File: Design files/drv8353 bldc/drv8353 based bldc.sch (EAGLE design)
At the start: 123 parts, among them IC1 DRV8353RSRGZT, J3 2X6 FEMALE, J4 B06B-HCMKK

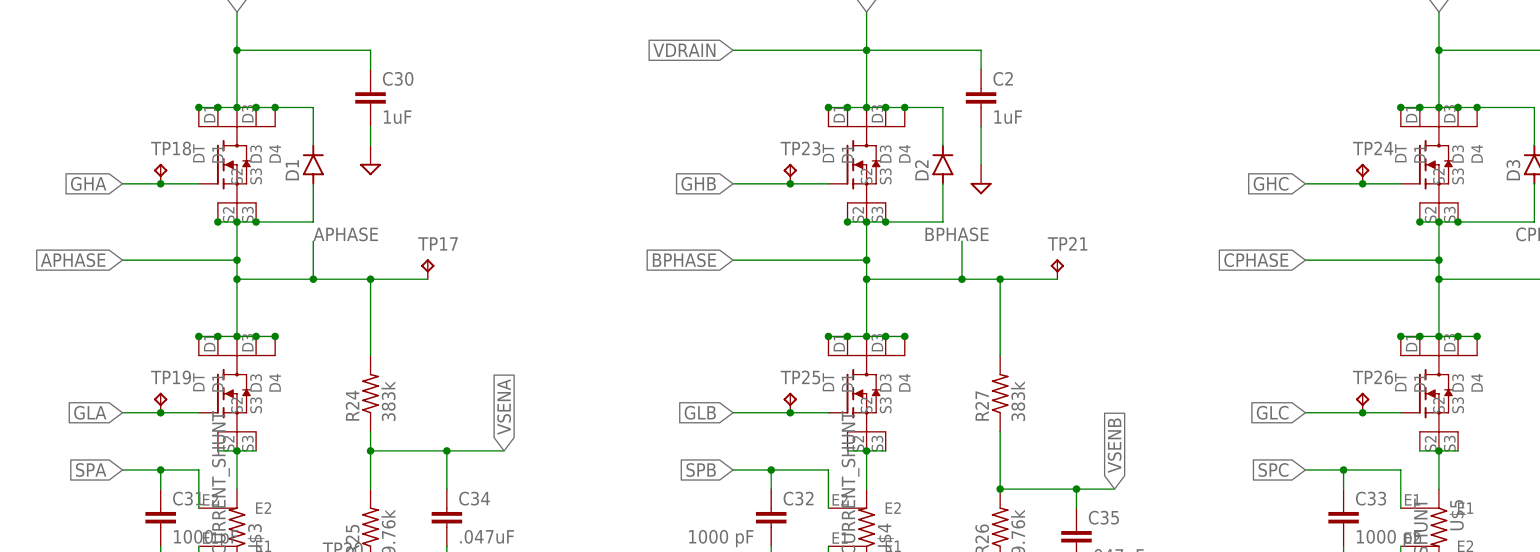
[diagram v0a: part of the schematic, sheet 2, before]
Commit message: placed most test points
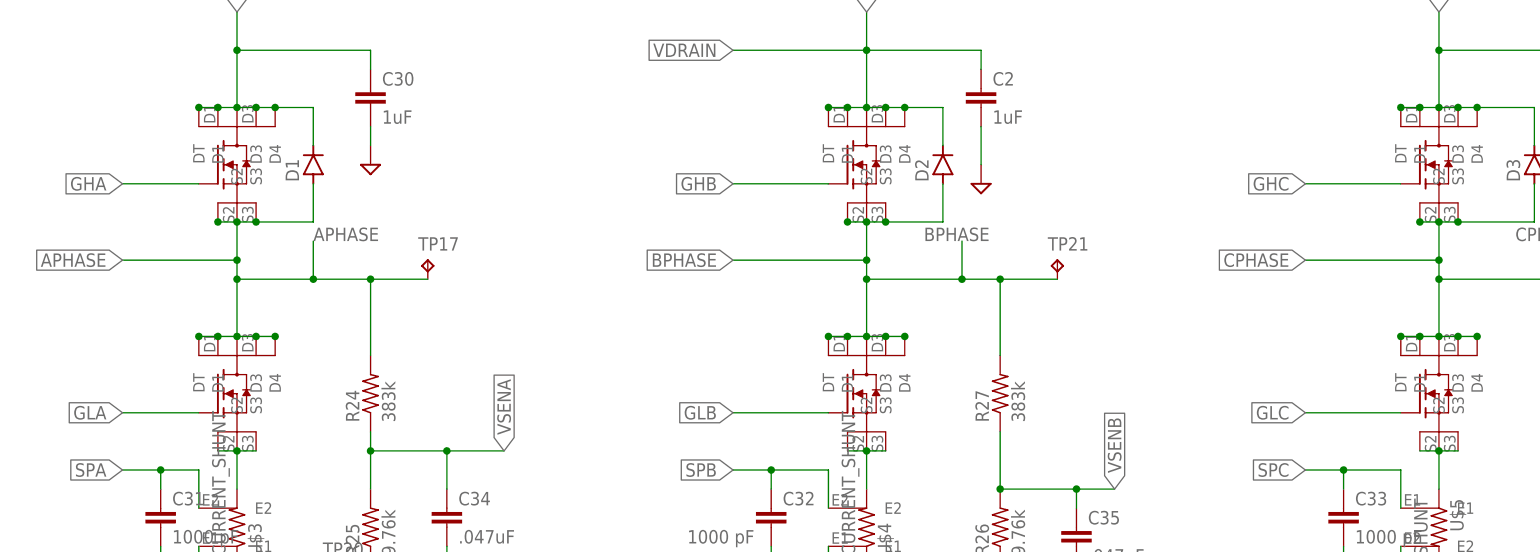
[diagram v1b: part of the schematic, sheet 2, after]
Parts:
- removed TP19, TP23, TP24, TP25, TP26: TPB1,27, testpad:TPB1,27
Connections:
- net GHA: no longer TP18.TP
- net GHB: no longer TP23.TP
- net GHC: no longer TP24.TP
- net GLA: no longer TP19.TP
- net GLB: no longer TP25.TP
- net GLC: no longer TP26.TP
- net SOA: now also TP18.TP
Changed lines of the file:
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@@
 <part name="U$24" library="REV BLDC" deviceset="NVMTS1D2N08H" device=""/>
 <part name="TP17" library="testpad" library_urn="urn:adsk.eagle:library:385" deviceset="TP" device="B1,27" package3d_urn="urn:adsk.eagle:package:27944/2"/>
-<part name="TP18" library="testpad" library_urn="urn:adsk.eagle:library:385" deviceset="TP" device="B1,27" package3d_urn="urn:adsk.eagle:package:27944/2"/>
-<part name="TP19" library="testpad" library_urn="urn:adsk.eagle:library:385" deviceset="TP" device="B1,27" package3d_urn="urn:adsk.eagle:package:27944/2"/>
 <part name="C30" library="rcl" library_urn="urn:adsk.eagle:library:334" deviceset="C-EU" device="C1206" package3d_urn="urn:adsk.eagle:package:23618/2" value="1uF"/>
 <part name="C31" library="rcl" library_urn="urn:adsk.eagle:library:334" deviceset="C-EU" device="C0603K" package3d_urn="urn:adsk.eagle:package:23680/2" value="1000 pF"/>
@@
 <part name="R29" library="rcl" library_urn="urn:adsk.eagle:library:334" deviceset="R-US_" device="R0603" package3d_urn="urn:adsk.eagle:package:23555/3" value="9.76k"/>
 <part name="C36" library="rcl" library_urn="urn:adsk.eagle:library:334" deviceset="C-EU" device="C0603K" package3d_urn="urn:adsk.eagle:package:23680/2" value=".047uF"/>
-<part name="TP23" library="testpad" library_urn="urn:adsk.eagle:library:385" deviceset="TP" device="B1,27" package3d_urn="urn:adsk.eagle:package:27944/2"/>
-<part name="TP24" library="testpad" library_urn="urn:adsk.eagle:library:385" deviceset="TP" device="B1,27" package3d_urn="urn:adsk.eagle:package:27944/2"/>
-<part name="TP25" library="testpad" library_urn="urn:adsk.eagle:library:385" deviceset="TP" device="B1,27" package3d_urn="urn:adsk.eagle:package:27944/2"/>
-<part name="TP26" library="testpad" library_urn="urn:adsk.eagle:library:385" deviceset="TP" device="B1,27" package3d_urn="urn:adsk.eagle:package:27944/2"/>
 <part name="TP27" library="testpad" library_urn="urn:adsk.eagle:library:385" deviceset="TP" device="B1,27" package3d_urn="urn:adsk.eagle:package:27944/2"/>
 <part name="TP28" library="testpad" library_urn="urn:adsk.eagle:library:385" deviceset="TP" device="B1,27" package3d_urn="urn:adsk.eagle:package:27944/2"/>
@@
 <part name="C3" library="rcl" library_urn="urn:adsk.eagle:library:334" deviceset="C-EU" device="C1206" package3d_urn="urn:adsk.eagle:package:23618/2" value="1uF"/>
 <part name="TP40" library="testpad" library_urn="urn:adsk.eagle:library:385" deviceset="TP" device="B1,27" package3d_urn="urn:adsk.eagle:package:27944/2"/>
+<part name="TP18" library="testpad" library_urn="urn:adsk.eagle:library:385" deviceset="TP" device="B1,27" package3d_urn="urn:adsk.eagle:package:27944/2"/>
 </parts>
 <sheets>
@@
 <attribute name="TP_SIGNAL_NAME" x="-67.31" y="-82.55" size="1.778" layer="97"/>
 </instance>
+<instance part="TP18" gate="G$1" x="48.26" y="-71.12" smashed="yes" rot="R180">
+<attribute name="NAME" x="49.53" y="-72.39" size="1.778" layer="95" rot="R180"/>
+<attribute name="TP_SIGNAL_NAME" x="46.99" y="-69.85" size="1.778" layer="97" rot="R180"/>
+</instance>
 </instances>
 <busses>
@@
 <wire x1="43.18" y1="-68.58" x2="48.26" y2="-68.58" width="0.1524" layer="91"/>
 <label x="48.26" y="-68.58" size="1.778" layer="95"/>
+<pinref part="TP18" gate="G$1" pin="TP"/>
 </segment>
 </net>
@@
 <attribute name="TP_SIGNAL_NAME" x="-29.21" y="46.99" size="1.778" layer="97"/>
 </instance>
-<instance part="TP18" gate="G$1" x="-66.04" y="60.96" smashed="yes">
-<attribute name="NAME" x="-67.31" y="62.23" size="1.778" layer="95"/>
-<attribute name="TP_SIGNAL_NAME" x="-64.77" y="59.69" size="1.778" layer="97"/>
-</instance>
-<instance part="TP19" gate="G$1" x="-66.04" y="30.48" smashed="yes">
-<attribute name="NAME" x="-67.31" y="31.75" size="1.778" layer="95"/>
-<attribute name="TP_SIGNAL_NAME" x="-64.77" y="29.21" size="1.778" layer="97"/>
-</instance>
 <instance part="C30" gate="G$1" x="-38.1" y="71.12" smashed="yes">
 <attribute name="NAME" x="-36.576" y="71.501" size="1.778" layer="95"/>
@@
 <attribute name="NAME" x="141.224" y="15.621" size="1.778" layer="95"/>
 <attribute name="VALUE" x="141.224" y="10.541" size="1.778" layer="96"/>
-</instance>
-<instance part="TP23" gate="G$1" x="17.78" y="60.96" smashed="yes">
-<attribute name="NAME" x="16.51" y="62.23" size="1.778" layer="95"/>
-<attribute name="TP_SIGNAL_NAME" x="19.05" y="59.69" size="1.778" layer="97"/>
-</instance>
-<instance part="TP24" gate="G$1" x="93.98" y="60.96" smashed="yes">
-<attribute name="NAME" x="92.71" y="62.23" size="1.778" layer="95"/>
-<attribute name="TP_SIGNAL_NAME" x="95.25" y="59.69" size="1.778" layer="97"/>
-</instance>
-<instance part="TP25" gate="G$1" x="17.78" y="30.48" smashed="yes">
-<attribute name="NAME" x="16.51" y="31.75" size="1.778" layer="95"/>
-<attribute name="TP_SIGNAL_NAME" x="19.05" y="29.21" size="1.778" layer="97"/>
-</instance>
-<instance part="TP26" gate="G$1" x="93.98" y="30.48" smashed="yes">
-<attribute name="NAME" x="92.71" y="31.75" size="1.778" layer="95"/>
-<attribute name="TP_SIGNAL_NAME" x="95.25" y="29.21" size="1.778" layer="97"/>
 </instance>
 <instance part="TP27" gate="G$1" x="40.64" y="7.62" smashed="yes">
@@
 <segment>
 <pinref part="U$14" gate="G$1" pin="G"/>
-<wire x1="-60.96" y1="58.42" x2="-66.04" y2="58.42" width="0.1524" layer="91"/>
-<pinref part="TP18" gate="G$1" pin="TP"/>
-<wire x1="-66.04" y1="58.42" x2="-71.12" y2="58.42" width="0.1524" layer="91"/>
-<junction x="-66.04" y="58.42"/>
+<wire x1="-60.96" y1="58.42" x2="-71.12" y2="58.42" width="0.1524" layer="91"/>
 <label x="-71.12" y="58.42" size="1.778" layer="95" rot="R180" xref="yes"/>
 </segment>
@@
 <segment>
 <pinref part="U$20" gate="G$1" pin="G"/>
-<wire x1="-60.96" y1="27.94" x2="-66.04" y2="27.94" width="0.1524" layer="91"/>
-<pinref part="TP19" gate="G$1" pin="TP"/>
-<wire x1="-66.04" y1="27.94" x2="-71.12" y2="27.94" width="0.1524" layer="91"/>
-<junction x="-66.04" y="27.94"/>
+<wire x1="-60.96" y1="27.94" x2="-71.12" y2="27.94" width="0.1524" layer="91"/>
 <label x="-71.12" y="27.94" size="1.778" layer="95" rot="R180" xref="yes"/>
 </segment>
@@
 <segment>
 <pinref part="U$22" gate="G$1" pin="G"/>
-<wire x1="22.86" y1="58.42" x2="17.78" y2="58.42" width="0.1524" layer="91"/>
-<pinref part="TP23" gate="G$1" pin="TP"/>
-<wire x1="17.78" y1="58.42" x2="10.16" y2="58.42" width="0.1524" layer="91"/>
-<junction x="17.78" y="58.42"/>
+<wire x1="22.86" y1="58.42" x2="10.16" y2="58.42" width="0.1524" layer="91"/>
 <label x="10.16" y="58.42" size="1.778" layer="95" rot="R180" xref="yes"/>
 </segment>
@@
 <segment>
 <pinref part="U$21" gate="G$1" pin="G"/>
-<wire x1="22.86" y1="27.94" x2="17.78" y2="27.94" width="0.1524" layer="91"/>
-<pinref part="TP25" gate="G$1" pin="TP"/>
-<wire x1="17.78" y1="27.94" x2="10.16" y2="27.94" width="0.1524" layer="91"/>
-<junction x="17.78" y="27.94"/>
+<wire x1="22.86" y1="27.94" x2="10.16" y2="27.94" width="0.1524" layer="91"/>
 <label x="10.16" y="27.94" size="1.778" layer="95" rot="R180" xref="yes"/>
 </segment>
@@
 <segment>
 <pinref part="U$24" gate="G$1" pin="G"/>
-<wire x1="99.06" y1="27.94" x2="93.98" y2="27.94" width="0.1524" layer="91"/>
-<pinref part="TP26" gate="G$1" pin="TP"/>
-<wire x1="93.98" y1="27.94" x2="86.36" y2="27.94" width="0.1524" layer="91"/>
-<junction x="93.98" y="27.94"/>
+<wire x1="99.06" y1="27.94" x2="86.36" y2="27.94" width="0.1524" layer="91"/>
 <label x="86.36" y="27.94" size="1.778" layer="95" rot="R180" xref="yes"/>
 </segment>
@@
 <segment>
 <pinref part="U$23" gate="G$1" pin="G"/>
-<wire x1="99.06" y1="58.42" x2="93.98" y2="58.42" width="0.1524" layer="91"/>
-<pinref part="TP24" gate="G$1" pin="TP"/>
-<wire x1="93.98" y1="58.42" x2="86.36" y2="58.42" width="0.1524" layer="91"/>
-<junction x="93.98" y="58.42"/>
+<wire x1="99.06" y1="58.42" x2="86.36" y2="58.42" width="0.1524" layer="91"/>
 <label x="86.36" y="58.42" size="1.778" layer="95" rot="R180" xref="yes"/>
 </segment>

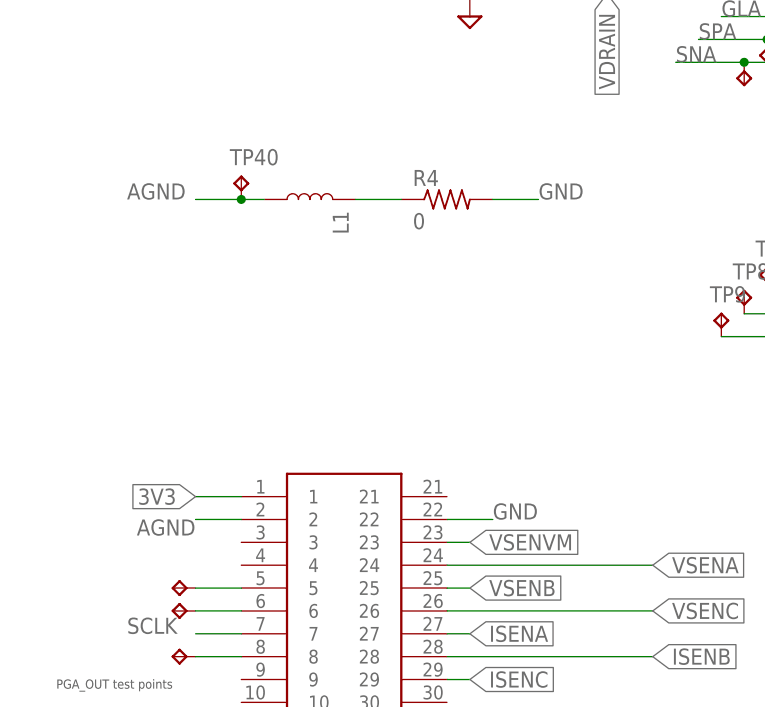
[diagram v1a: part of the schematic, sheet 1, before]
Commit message: fixes: c31-33 closer to fets, spacing of ABCPhases, layout of drv internal buck regulator
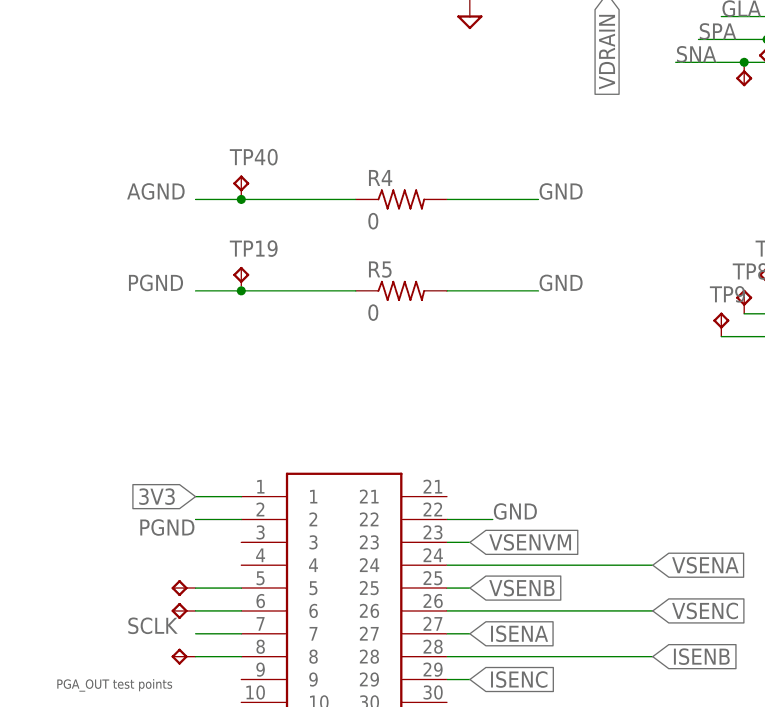
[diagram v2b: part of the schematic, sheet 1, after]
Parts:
- removed L1: 33nH/±5%/500mA, SparkFun-Coils:INDUCTOR-0603-33NH
- added R5: 0, resistor:R-US_R0603
- added TP19: TPB1,27, testpad:TPB1,27
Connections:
- removed net N$21: L1.2, R4.1
- new net PGND: R5.1, TP19.TP, U$2.2
- net AGND: now also R4.1; no longer L1.1, U$2.2
- net GND: now also R5.2
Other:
- moved on the sheet: R4
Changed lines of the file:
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@@
 <?xml version="1.0" encoding="utf-8"?>
 <!DOCTYPE eagle SYSTEM "eagle.dtd">
-<eagle version="9.5.0">
+<eagle version="9.5.1">
 <drawing>
 <settings>
@@
 <part name="SUPPLY11" library="supply2" library_urn="urn:adsk.eagle:library:372" deviceset="GND" device=""/>
 <part name="R3" library="resistor" library_urn="urn:adsk.eagle:library:348" deviceset="R-US_" device="R0603" package3d_urn="urn:adsk.eagle:package:26057/1" value="5K"/>
-<part name="L1" library="SparkFun-Coils" library_urn="urn:adsk.eagle:library:512" deviceset="INDUCTOR" device="-0603-33NH" package3d_urn="urn:adsk.eagle:package:37574/1" value="33nH/±5%/500mA"/>
 <part name="R4" library="resistor" library_urn="urn:adsk.eagle:library:348" deviceset="R-US_" device="R0603" package3d_urn="urn:adsk.eagle:package:26057/1" value="0"/>
 <part name="U$3" library="REV BLDC" deviceset="CURRENT_SHUNT" device=""/>
@@
 <part name="TP40" library="testpad" library_urn="urn:adsk.eagle:library:385" deviceset="TP" device="B1,27" package3d_urn="urn:adsk.eagle:package:27944/2"/>
 <part name="TP18" library="testpad" library_urn="urn:adsk.eagle:library:385" deviceset="TP" device="B1,27" package3d_urn="urn:adsk.eagle:package:27944/2"/>
+<part name="R5" library="resistor" library_urn="urn:adsk.eagle:library:348" deviceset="R-US_" device="R0603" package3d_urn="urn:adsk.eagle:package:26057/1" value="0"/>
+<part name="TP19" library="testpad" library_urn="urn:adsk.eagle:library:385" deviceset="TP" device="B1,27" package3d_urn="urn:adsk.eagle:package:27944/2"/>
 </parts>
 <sheets>
@@
 <attribute name="VALUE" x="92.71" y="-127.762" size="1.778" layer="96"/>
 </instance>
-<instance part="L1" gate="G$1" x="-60.96" y="-83.82" smashed="yes" rot="R90">
-<attribute name="NAME" x="-58.42" y="-85.09" size="1.778" layer="95" rot="R270"/>
-</instance>
-<instance part="R4" gate="G$1" x="-45.72" y="-83.82" smashed="yes">
-<attribute name="NAME" x="-49.53" y="-82.3214" size="1.778" layer="95"/>
-<attribute name="VALUE" x="-49.53" y="-87.122" size="1.778" layer="96"/>
+<instance part="R4" gate="G$1" x="-50.8" y="-83.82" smashed="yes">
+<attribute name="NAME" x="-54.61" y="-82.3214" size="1.778" layer="95"/>
+<attribute name="VALUE" x="-54.61" y="-87.122" size="1.778" layer="96"/>
 </instance>
 <instance part="TP40" gate="G$1" x="-68.58" y="-81.28" smashed="yes">
@@
 <attribute name="NAME" x="49.53" y="-72.39" size="1.778" layer="95" rot="R180"/>
 <attribute name="TP_SIGNAL_NAME" x="46.99" y="-69.85" size="1.778" layer="97" rot="R180"/>
+</instance>
+<instance part="R5" gate="G$1" x="-50.8" y="-93.98" smashed="yes">
+<attribute name="NAME" x="-54.61" y="-92.4814" size="1.778" layer="95"/>
+<attribute name="VALUE" x="-54.61" y="-97.282" size="1.778" layer="96"/>
+</instance>
+<instance part="TP19" gate="G$1" x="-68.58" y="-91.44" smashed="yes">
+<attribute name="NAME" x="-69.85" y="-90.17" size="1.778" layer="95"/>
+<attribute name="TP_SIGNAL_NAME" x="-67.31" y="-92.71" size="1.778" layer="97"/>
 </instance>
 </instances>
@@
 <segment>
 <pinref part="R4" gate="G$1" pin="2"/>
-<wire x1="-40.64" y1="-83.82" x2="-35.56" y2="-83.82" width="0.1524" layer="91"/>
+<wire x1="-45.72" y1="-83.82" x2="-35.56" y2="-83.82" width="0.1524" layer="91"/>
 <label x="-35.56" y="-83.82" size="1.778" layer="95"/>
 </segment>
@@
 <wire x1="93.98" y1="-88.9" x2="96.52" y2="-88.9" width="0.1524" layer="91"/>
 <label x="96.52" y="-88.9" size="1.778" layer="95"/>
+</segment>
+<segment>
+<pinref part="R5" gate="G$1" pin="2"/>
+<wire x1="-45.72" y1="-93.98" x2="-35.56" y2="-93.98" width="0.1524" layer="91"/>
+<label x="-35.56" y="-93.98" size="1.778" layer="95"/>
 </segment>
 </net>
@@
 </segment>
 <segment>
-<pinref part="L1" gate="G$1" pin="1"/>
-<wire x1="-66.04" y1="-83.82" x2="-68.58" y2="-83.82" width="0.1524" layer="91"/>
 <label x="-81.28" y="-83.82" size="1.778" layer="95"/>
 <pinref part="TP40" gate="G$1" pin="TP"/>
 <wire x1="-68.58" y1="-83.82" x2="-73.66" y2="-83.82" width="0.1524" layer="91"/>
 <junction x="-68.58" y="-83.82"/>
-</segment>
-<segment>
-<wire x1="-68.58" y1="-119.38" x2="-73.66" y2="-119.38" width="0.1524" layer="91"/>
-<label x="-73.66" y="-119.38" size="1.778" layer="95" rot="R180"/>
-<pinref part="U$2" gate="G$1" pin="2"/>
+<pinref part="R4" gate="G$1" pin="1"/>
+<wire x1="-68.58" y1="-83.82" x2="-55.88" y2="-83.82" width="0.1524" layer="91"/>
 </segment>
 </net>
@@
 </segment>
 </net>
-<net name="N$21" class="0">
-<segment>
-<pinref part="L1" gate="G$1" pin="2"/>
-<pinref part="R4" gate="G$1" pin="1"/>
-<wire x1="-55.88" y1="-83.82" x2="-50.8" y2="-83.82" width="0.1524" layer="91"/>
-</segment>
-</net>
 <net name="ISENA" class="0">
 <segment>
@@
 </segment>
 </net>
+<net name="PGND" class="0">
+<segment>
+<label x="-81.28" y="-93.98" size="1.778" layer="95"/>
+<pinref part="TP19" gate="G$1" pin="TP"/>
+<wire x1="-68.58" y1="-93.98" x2="-73.66" y2="-93.98" width="0.1524" layer="91"/>
+<junction x="-68.58" y="-93.98"/>
+<pinref part="R5" gate="G$1" pin="1"/>
+<wire x1="-68.58" y1="-93.98" x2="-55.88" y2="-93.98" width="0.1524" layer="91"/>
+</segment>
+<segment>
+<wire x1="-68.58" y1="-119.38" x2="-73.66" y2="-119.38" width="0.1524" layer="91"/>
+<label x="-73.66" y="-119.38" size="1.778" layer="95" rot="R180"/>
+<pinref part="U$2" gate="G$1" pin="2"/>
+</segment>
+</net>
